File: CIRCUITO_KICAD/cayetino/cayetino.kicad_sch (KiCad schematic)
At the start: 0 parts

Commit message: Refactor code structure for improved readability and maintainability
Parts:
- added A1: RaspberryPi_Pico, Module:RaspberryPi_Pico_SMD_only_pins, symbol MCU_Module:RaspberryPi_Pico_Extensive
- added A2: Arduino_Uno_R3_Shield, PCM_arduino-library:Arduino_Uno_R3_only_headers, symbol PCM_arduino-library:Arduino_Uno_R3_Shield
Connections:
- new net: A1.36 (3V3), A2.3V3 (3.3V)
- new net: A1.31 (GPIO26_ADC0), A2.A0
- new net: A1.32 (GPIO27_ADC1), A2.A1
- new net: A1.34 (GPIO28_ADC2), A2.A2
- new net: A1.1 (GPIO0), A2.D0 (D0/RX)
- new net: A1.2 (GPIO1), A2.D1 (D1/TX)
- new net: A1.14 (GPIO10), A2.D10 (D10_CS)
- new net: A1.15 (GPIO11), A2.D11
- new net: A1.16 (GPIO12), A2.D12
- new net: A1.17 (GPIO13), A2.D13
- new net: A1.4 (GPIO2), A2.D2 (D2_INT0)
- new net: A1.5 (GPIO3), A2.D3 (D3_INT1)
- new net: A1.6 (GPIO4), A2.D4
- new net: A1.7 (GPIO5), A2.D5
- new net: A1.9 (GPIO6), A2.D6
- new net: A1.10 (GPIO7), A2.D7
- new net: A1.11 (GPIO8), A2.D8
- new net: A1.12 (GPIO9), A2.D9
- new net: A1.13 (GND), A1.18 (GND), A1.23 (GND), A1.28 (GND), A1.3 (GND), A1.38 (GND), A1.8 (GND), A1.D2 (GND), A2.GND1 (GND), A2.GND2 (GND), A2.GND3 (GND)
- new net: A1.30 (RUN), A2.RST1 (RESET)

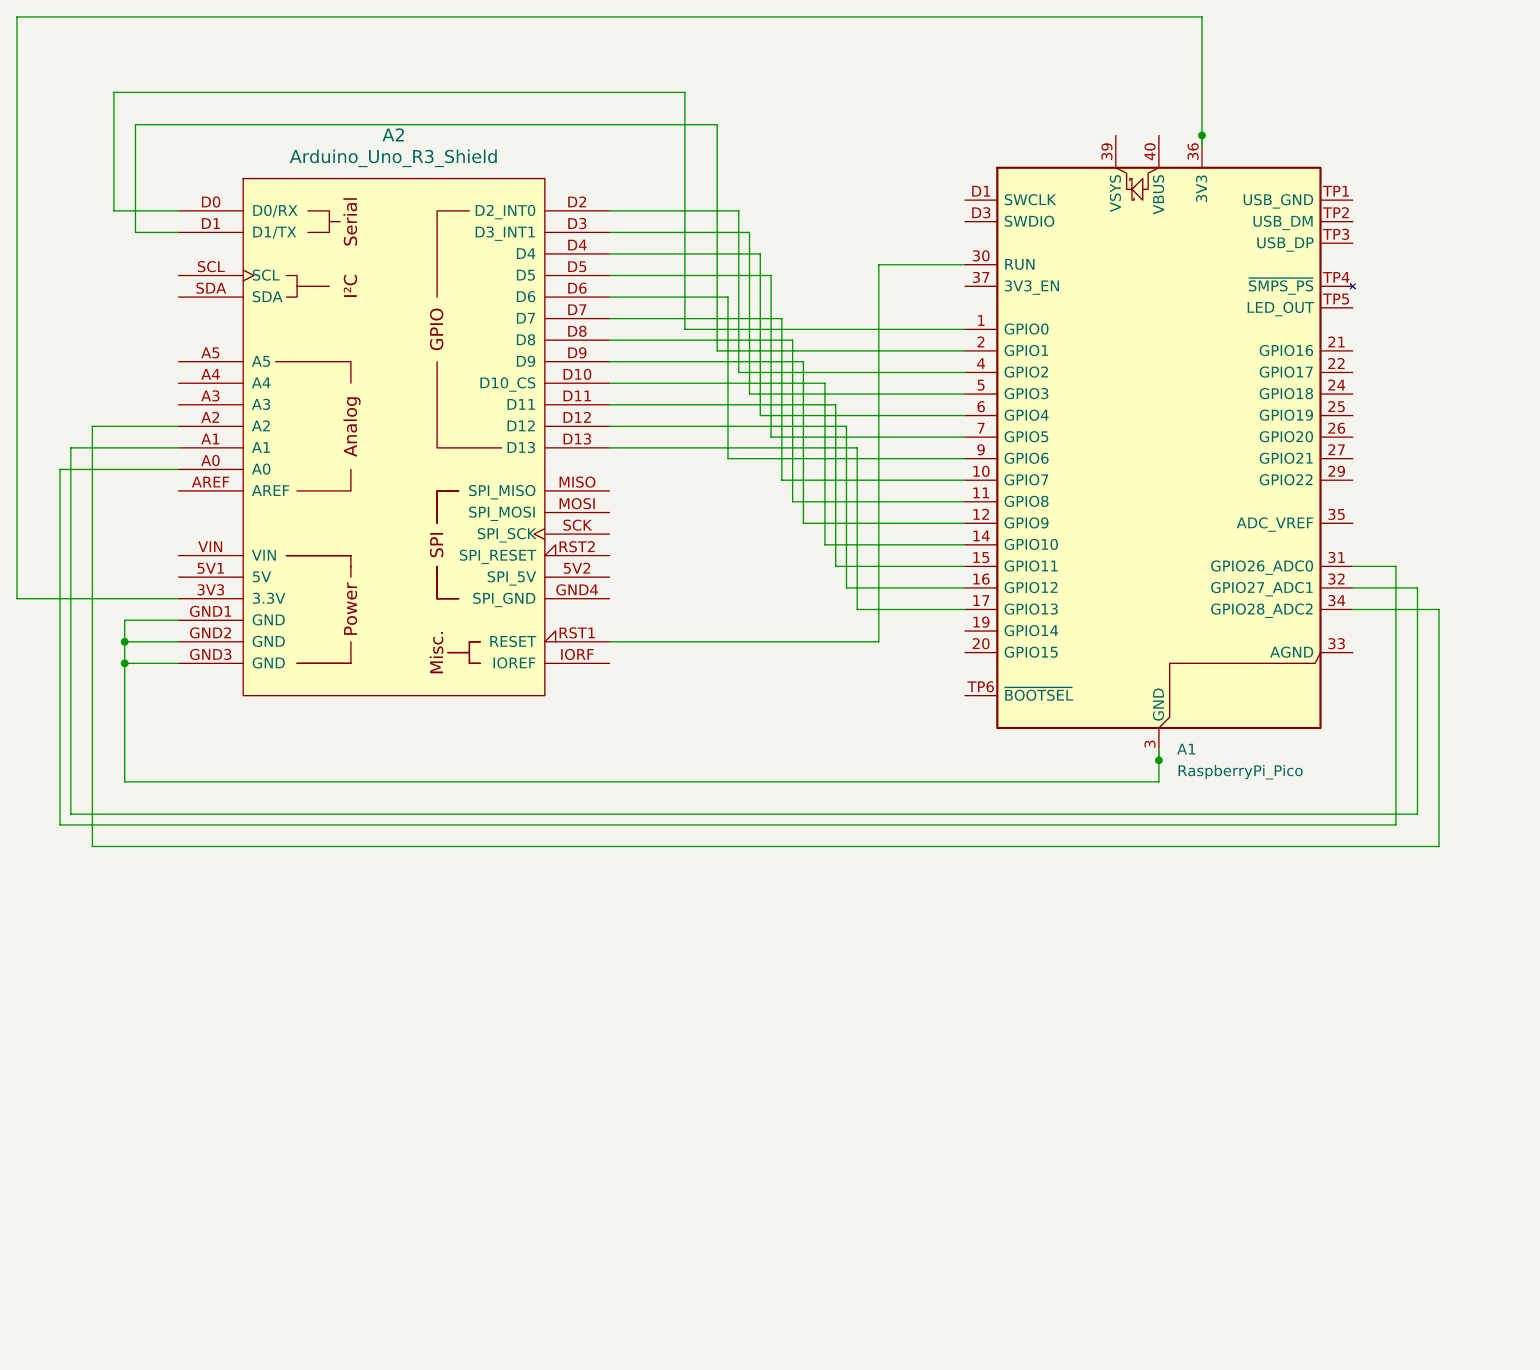
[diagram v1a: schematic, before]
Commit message: Add Micro SD Card Socket with detection pin to Cayetino project
- Updated `cayetino.kicad_pro` to include new designator for the Micro SD Card Socket (J1).
- Added Micro SD Card Socket symbol and properties in `cayetino.kicad_sch`.
- Included necessary pin configurations and labels for the Micro SD Card Socket.
- Created a new `report.txt` file for project documentation.
- Added a lock file `~cayetino.kicad_pro.lck` for project management.
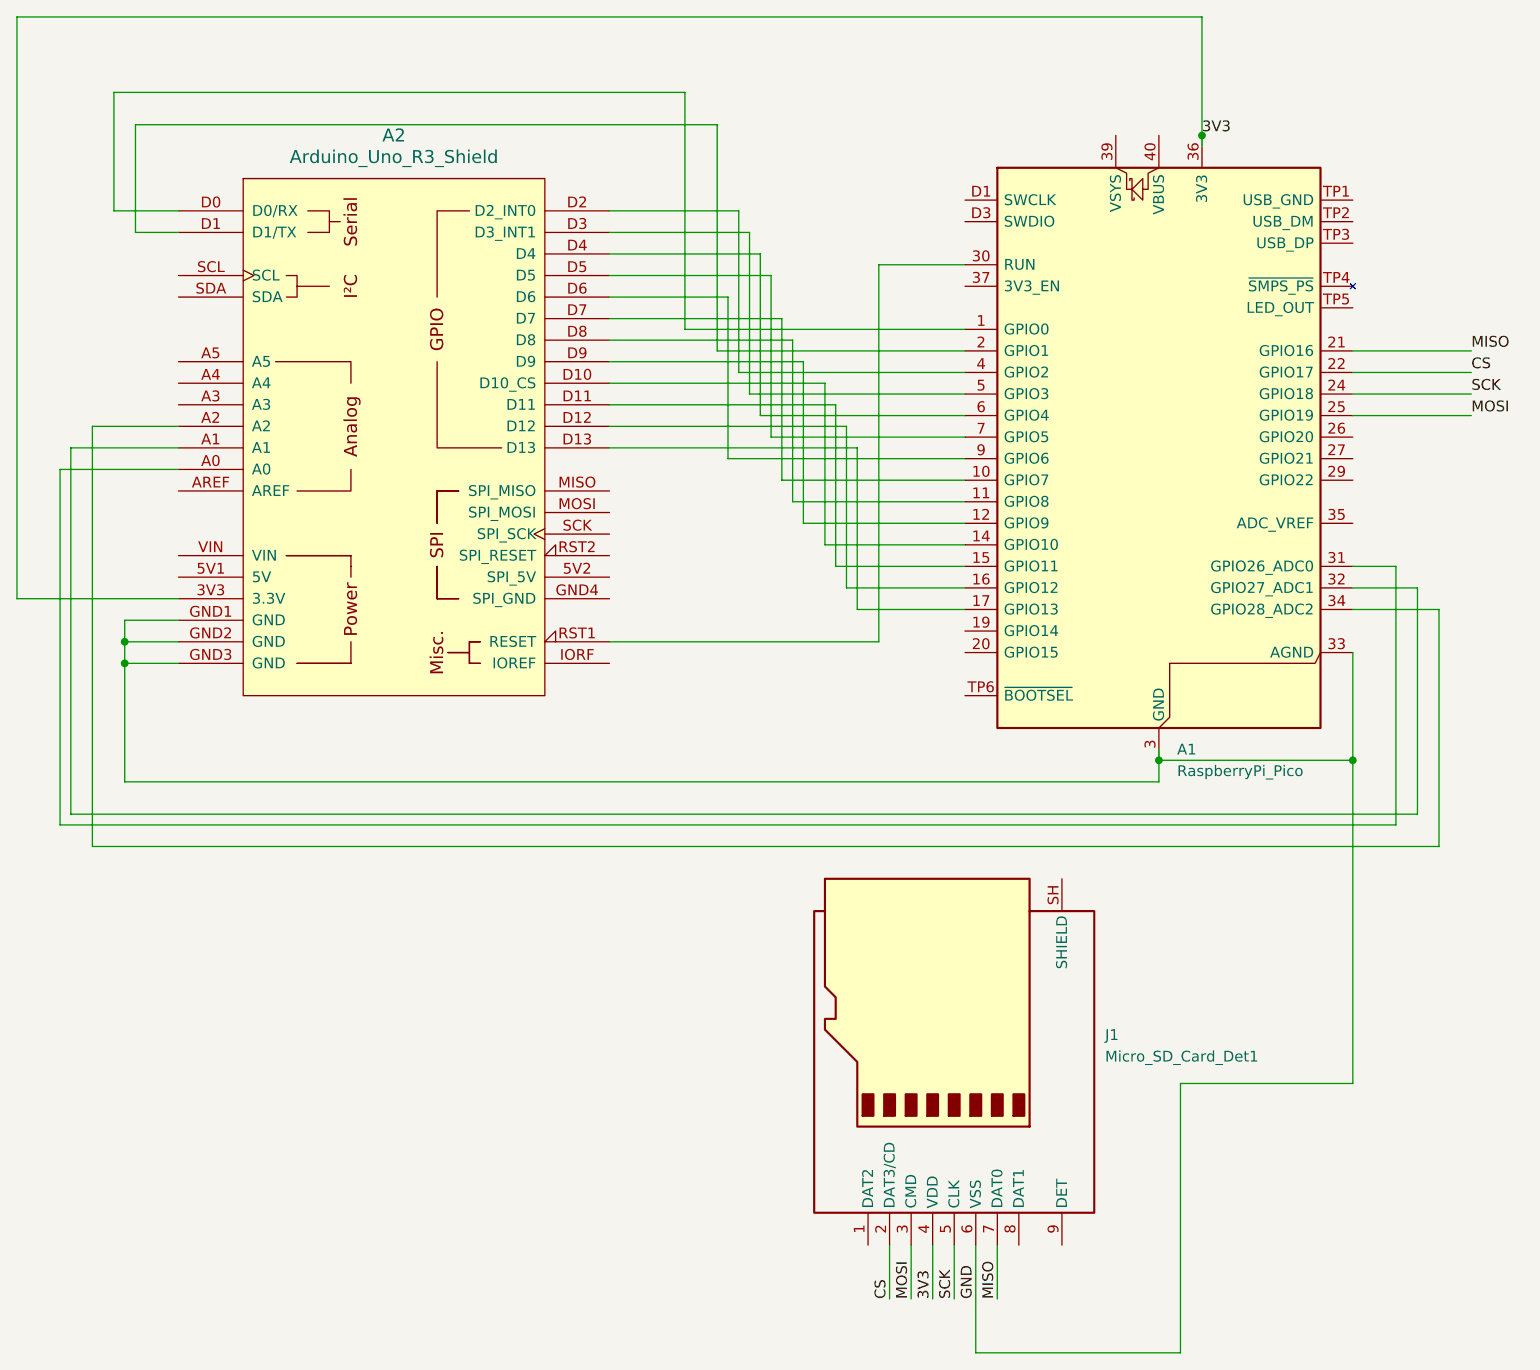
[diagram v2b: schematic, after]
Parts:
- added J1: Micro_SD_Card_Det1, Module:J_SD_Card-micro_socket_A, symbol Connector:Micro_SD_Card_Det1
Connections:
- net 3V3: now reaches A1.36 (3V3), A2.3V3 (3.3V)
- net 3V3: now also J1.4 (VDD)
- net GND: now reaches A1.13 (GND), A1.18 (GND), A1.23 (GND), A1.28 (GND), A1.3 (GND), A1.38 (GND), A1.8 (GND), A1.D2 (GND), A2.GND1 (GND), A2.GND2 (GND), A2.GND3 (GND)
- net GND: now also A1.33 (AGND), J1.6 (VSS)
- net MISO: now reaches A1.21 (GPIO16)
- net MISO: now also J1.7 (DAT0)
- net CS: now reaches A1.22 (GPIO17)
- net CS: now also J1.2 (DAT3/CD)
- net SCK: now reaches A1.24 (GPIO18)
- net SCK: now also J1.5 (CLK)
- net MOSI: now reaches A1.25 (GPIO19)
- net MOSI: now also J1.3 (CMD)
